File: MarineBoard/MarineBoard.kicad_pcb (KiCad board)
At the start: 4 copper layers, 83 x 67.5 mm, 157 parts, among them CN1 MKDSN 1,5/ 2-5,08, CN2 MKDSN 1,5/ 2-5,08, CN3 SM04B-SRSS-TB (LF)(SN), J1 USB_C_Receptacle_USB2.0_16P, Q2 S8050, Q3 S8050, Q4 BUK762R4-60E, U1 SY8089A1AAC, U10 SM10B-GHS-TB, U11 SN65HVD230DR, U12 DB125-3.5-3P-GN-S, U13 DB125-3.5-3P-GN-S, U14 PC817C-S, U16 PC817C-S, U17 PC817C-S, U18 INA226, U19 INA226, U2 INA226, U21 PC817C-S, U22 SN74LVC1G14DBVR, U23 MCP1407-E/MF_C640313, U3 TPS5430DDA, U4 DB125-3.5-2P-GN-S, U5 DB125-3.5-2P-GN-S, U6 DB125-3.5-2P-GN-S, U7 DB125-3.5-3P-GN-S, U8 ESP32-S3-WROOM-2-N32R16V, U9 DB125-3.5-3P-GN-S

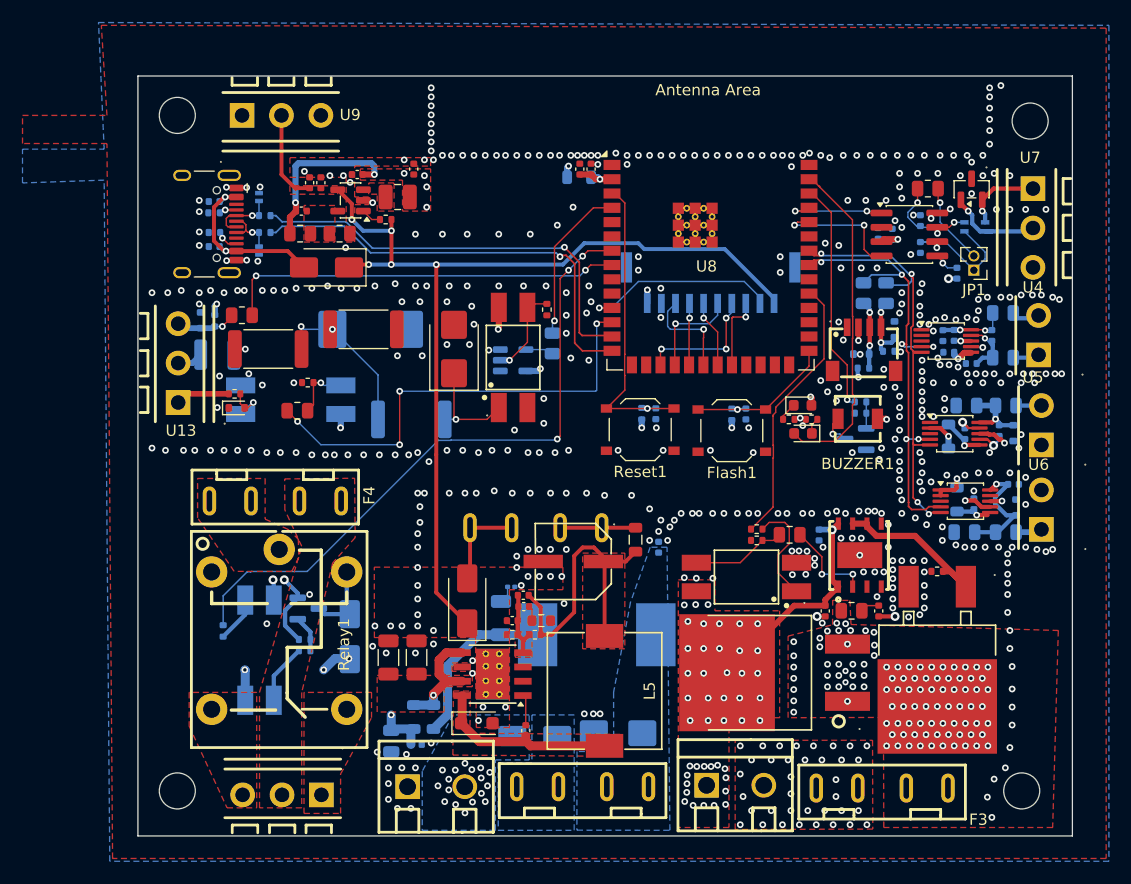
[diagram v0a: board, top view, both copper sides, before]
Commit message: MarineBoard v1.9: RGB status LED, vertical CN4 display header, logo, fab package (#179)
- D17 plain LED -> D5 WS2812B-2020-V6 (C52917434) on GPIO1, VDD +5V_VCC,
  C40 decoupling, R34 100R on DIN
- U10 right-angle GH on the bottom -> CN4 vertical BM10B-GHS-TBT on top
  (pinout unchanged); all fuses/connectors on top; GND stitching reworked
- Sisu logo + "MARINE BOARD v1.9" silk (LOGO1), RESET/FLASH labels
- Libraries consolidated back into Lib/ (root EasyEDA.* retired), CN4
  courtyard now covers its leads, L2 footprint attr THT -> SMD
- fab_package.py rebuilds production/ (DRC gate, gerbers/drill/IPC zip,
  BOM + centroid CSV/XLSX with LOOSE rows); stale production files removed
- Technical Specs v1.9 (CN4, RGB LED, fab script, U5/U6/U7 pin order),
  system spec 2.15, README, feature map, HEADER PINS / LEDS exports

Firmware follow-up for the RGB LED: #180

Co-Authored-By: Claude Opus 5.5 <noreply@anthropic.com>
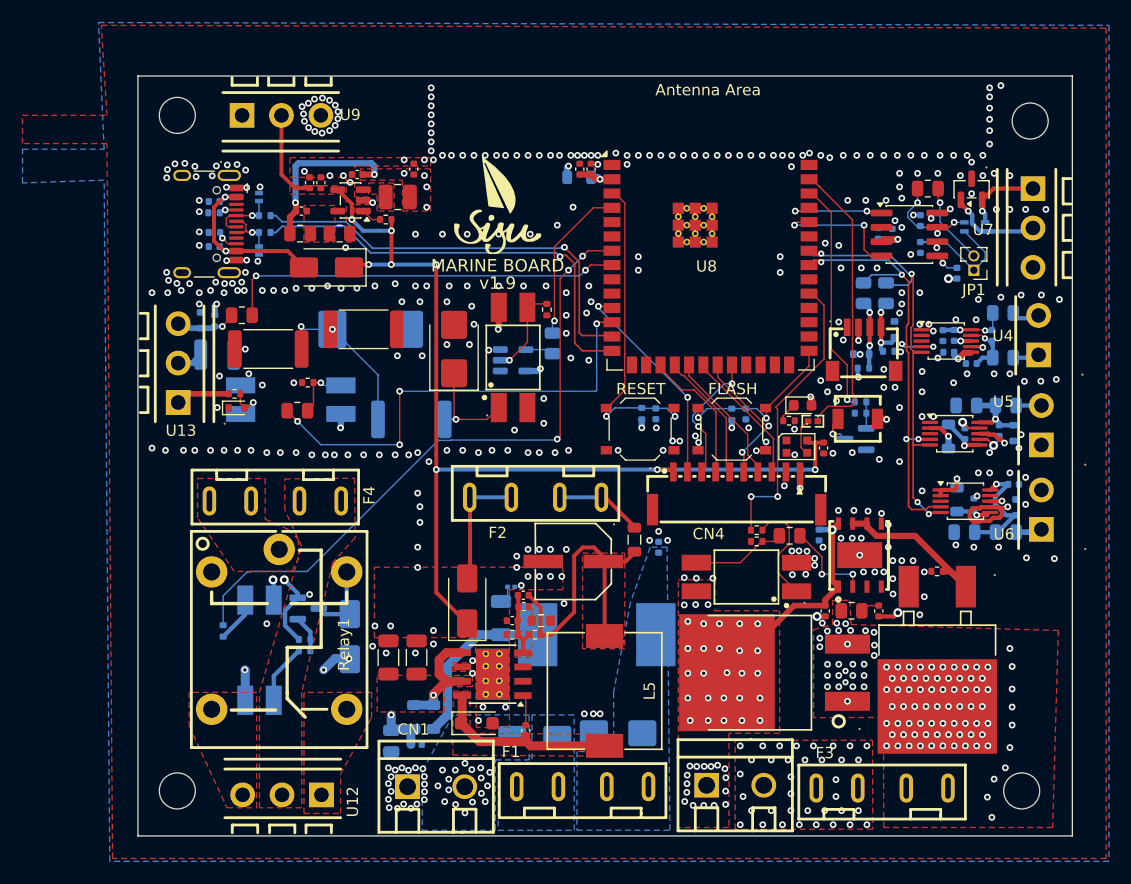
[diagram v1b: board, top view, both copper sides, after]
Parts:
- removed D17: LED, LED_SMD:LED_0603_1608Metric
- removed U10: SM10B-GHS-TB, LCSC:CONN-SMD_SM10B-GHS-TB
- added C40: 0.1uF, Capacitor_SMD:C_0402_1005Metric, F.Cu at (254.7, 70.8)
- added CN4: BM10B-GHS-TBT, LCSC:CONN-SMD_BM10B-GHS-TBT-LF-SN, F.Cu at (246.9, 74.6)
- added D5: WS2812B-2020, LED_SMD:LED_WS2812B-2020_PLCC4_2.0x2.0mm, F.Cu at (252.3, 70.7)
- added LOGO1: v1.9, LCSC:Sisu_Logo, F.Cu at (225.7, 50.8)
- F2: moved to F.Cu
- R34: value 470R -> 100; footprint Resistor_SMD:R_0402_1005Metric -> LCSC:R0402
- moved F2 2.71 mm to (229.1, 75.2)
- moved R34 0.20 mm to (253.7, 68.4), turned to 0 degrees
- moved Flash1 0.14 mm to (246.5, 69.1)
- moved R33 0.12 mm to (251.6, 68.4)
- moved L6 0.10 mm to (237.8, 78.9)
- moved R29 0.09 mm to (248.7, 78.1)
- moved R32 0.09 mm to (248.7, 79.1)
- moved R50 0.09 mm to (251.6, 78.6)
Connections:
- R34 pad 2: GND -> LED
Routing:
- net GND: track 18.4 -> 25.0 mm, vias 478 -> 417
- net MISO/GPIO13: track 5.98 -> 12.5 mm, vias 1 -> 2
- net MOSI/GPIO11: track 5.48 -> 11.9 mm, vias 1 -> 0
- net +5V_VCC: track 93.7 -> 99.5 mm, vias 5 -> 8
- net RST/GPIO14: track 6.64 -> 11.9 mm, vias 1 -> 2
- net LED: track 29.8 -> 26.0 mm
- net SCK/GPIO12: track 8.81 -> 12.0 mm, vias 1 -> 0
- net CS0/GPIO10: track 8.79 -> 11.5 mm, vias 1 -> 0
- net 5V_FUSED: track 8.30 -> 11.0 mm
- net Net-(D5-DIN): track 1.45 -> 3.39 mm
- net BL/GPIO18: track 17.5 -> 19.2 mm, vias 1 -> 2
- net BOOT: track 13.6 -> 15.1 mm, vias 1 -> 2
- net PWM1_GPIO: track 24.4 -> 25.9 mm, vias 0 -> 2
- net RESET: track 27.2 -> 28.6 mm, vias 1 -> 2
- net 5V_FILT: track 6.70 -> 7.85 mm
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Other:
- board text added: "FLASH"
- board text added: "RESET"

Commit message: MarineBoard v1.9.1 pre-fab fixes: U3 ENA float, 50V caps, polymer C20 (#183)
- U3 TPS5430 ENA (pin 5) disconnected from VIN_BUCK (7 V abs max) and left
  floating per TI; schematic wires + PCB stub removed, no-connect added.
- C11/C12/C14/C19/C42 -> CL05B104KB5NNNC (50 V; were 16 V on 12 V/bus nets),
  C33 -> 1 uF 50 V GRM155R61H105KE05D (was 4.7 uF 10 V on +12V BAT).
- C20 -> Panasonic 10SVPE220M 20 mOhm polymer: 15 uH + 220 uF <=40 mOhm is
  TI's internal-compensation reference; the copied ceramic-cap network
  C21/C22/R13/C23 (TI Fig 7-11, 3.3 V/100 uF design) is now DNP.
- Order sheet File Name -> MarineBoard-PCBWay-Gerbers.zip.
- Fab package rebuilt; DRC (schematic parity) and ERC unchanged vs before.

Still open in #183 (routing, human): U2 VBUS, U23 supply rail, C15, D5.

Co-Authored-By: Claude Opus 5.5 <noreply@anthropic.com>
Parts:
- C33: value 4.7uF -> 1uF
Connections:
- U3 pad 5: VIN_BUCK -> unconnected-(U3-EN-Pad5)
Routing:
- net VIN_BUCK: track 10.2 -> 5.75 mm
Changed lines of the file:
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@@
 			)
 		)
-		(property "Value" "4.7uF"
+		(property "Value" "1uF"
 			(at 0 1.16 90)
 			(layer "F.Fab")
@@
 			)
 		)
-		(property "Datasheet" "https://lcsc.com/product-detail/Multilayer-Ceramic-Capacitors-MLCC-SMD-SMT_SAMSUNG_CL05A475MP5NRNC_4-7uF-475-20-10V_C23733.html"
+		(property "Datasheet" "~"
 			(at 0 0 90)
 			(layer "F.Fab")
@@
 			)
 		)
-		(property "Description" "4.7uF ±20% 10V Ceramic Capacitor X5R 0402"
+		(property "Description" "1uF ±10% 50V Ceramic Capacitor X5R 0402"
 			(at 0 0 90)
 			(layer "F.Fab")
@@
 			)
 		)
-		(property "MPN" "CL05A475MP5NRNC"
+		(property "MPN" "GRM155R61H105KE05D"
 			(at 0 0 90)
 			(unlocked yes)
@@
 			)
 		)
-		(property "Manufacturer" "Samsung Electro-Mechanics"
+		(property "Manufacturer" "muRata"
 			(at 0 0 90)
 			(unlocked yes)
@@
 			(size 1.55 0.6)
 			(layers "F.Cu" "F.Mask" "F.Paste")
-			(net "VIN_BUCK")
+			(net "unconnected-(U3-EN-Pad5)")
 			(pinfunction "EN_5")
 			(pintype "input")
@@
 			)
 		)
-		(property "Datasheet" ""
+		(property "Datasheet" "~"
 			(at 0 0 0)
 			(layer "F.Fab")
@@
 			)
 		)
-		(property "Description" "220uF ±20% 10V Aluminum Electrolytic Capacitor 6.3x5.4mm"
+		(property "Description" "220uF ±20% 10V OS-CON polymer, ESR 20mΩ, SMD D6.3xL5.9mm (TPS5430 internal comp needs ESR <=40mΩ)"
 			(at 0 0 0)
 			(layer "F.Fab")
@@
 			)
 		)
-		(property "Manufacturer" "Lelon"
+		(property "Manufacturer" "Panasonic"
 			(at 0 0 180)
 			(unlocked yes)
@@
 			)
 		)
-		(property "MPN" "C72494"
+		(property "MPN" "10SVPE220M"
 			(at 0 0 180)
 			(unlocked yes)
@@
 			)
 		)
-		(attr smd)
+		(attr smd exclude_from_pos_files dnp)
 		(duplicate_pad_numbers_are_jumpers no)
 		(fp_line
@@
 			)
 		)
-		(attr smd)
+		(attr smd exclude_from_pos_files dnp)
 		(duplicate_pad_numbers_are_jumpers no)
 		(fp_line
@@
 			)
 		)
-		(attr smd)
+		(attr smd exclude_from_pos_files dnp)
 		(duplicate_pad_numbers_are_jumpers no)
 		(fp_line
@@
 			)
 		)
-		(attr smd)
+		(attr smd exclude_from_pos_files dnp)
 		(duplicate_pad_numbers_are_jumpers no)
 		(fp_line
@@
 			)
 		)
-		(property "Datasheet" "https://www.lcsc.com/datasheet/C1525.pdf"
+		(property "Datasheet" "~"
 			(at 0 0 90)
 			(layer "B.Fab")
@@
 			)
 		)
-		(property "Description" "Unpolarized capacitor"
+		(property "Description" "100nF ±10% 50V Ceramic Capacitor X7R 0402"
 			(at 0 0 90)
 			(layer "B.Fab")
@@
 			)
 		)
-		(property "MPN" "CL05B104KO5NNNC"
+		(property "MPN" "CL05B104KB5NNNC"
 			(at 0 0 270)
 			(unlocked yes)
@@
 			)
 		)
-		(property "Datasheet" "https://www.lcsc.com/datasheet/C1525.pdf"
+		(property "Datasheet" "~"
 			(at 0 0 90)
 			(layer "B.Fab")
@@
 			)
 		)
-		(property "Description" "Unpolarized capacitor"
+		(property "Description" "100nF ±10% 50V Ceramic Capacitor X7R 0402"
 			(at 0 0 90)
 			(layer "B.Fab")
@@
 			)
 		)
-		(property "MPN" "CL05B104KO5NNNC"
+		(property "MPN" "CL05B104KB5NNNC"
 			(at 0 0 90)
 			(unlocked yes)
@@
 			)
 		)
-		(property "Datasheet" ""
+		(property "Datasheet" "~"
 			(at 0 0 90)
 			(layer "B.Fab")
@@
 			)
 		)
-		(property "MPN" "CL05B104KO5NNNC"
+		(property "MPN" "CL05B104KB5NNNC"
 			(at 0 0 90)
 			(unlocked yes)
@@
 			)
 		)
-		(property "Datasheet" "https://www.lcsc.com/datasheet/C1525.pdf"
+		(property "Datasheet" "~"
 			(at 0 0 0)
 			(layer "B.Fab")
@@
 			)
 		)
-		(property "Description" "Unpolarized capacitor"
+		(property "Description" "100nF ±10% 50V Ceramic Capacitor X7R 0402"
 			(at 0 0 0)
 			(layer "B.Fab")
@@
 			)
 		)
-		(property "MPN" "CL05B104KO5NNNC"
+		(property "MPN" "CL05B104KB5NNNC"
 			(at 0 0 180)
 			(unlocked yes)
@@
 			)
 		)
-		(property "Datasheet" "https://www.lcsc.com/datasheet/C1525.pdf"
+		(property "Datasheet" "~"
 			(at 0 0 0)
 			(layer "B.Fab")
@@
 			)
 		)
-		(property "Description" "Unpolarized capacitor"
+		(property "Description" "100nF ±10% 50V Ceramic Capacitor X7R 0402"
 			(at 0 0 0)
 			(layer "B.Fab")
@@
 			)
 		)
-		(property "MPN" "CL05B104KO5NNNC"
+		(property "MPN" "CL05B104KB5NNNC"
 			(at 0 0 180)
 			(unlocked yes)
@@
 	)
 	(segment
-		(start 221.155 88.97)
-		(end 220.5 89.625)
-		(width 0.8)
-		(layer "F.Cu")
-		(net "VIN_BUCK")
-	)
-	(segment
-		(start 222.55 88.97)
-		(end 221.155 88.97)
-		(width 0.8)
-		(layer "F.Cu")
-		(net "VIN_BUCK")
-	)
-	(segment
 		(start 220 92.75)
 		(end 220 92.645)
 		(width 0.8)
 		(layer "F.Cu")
-		(net "VIN_BUCK")
-	)
-	(segment
-		(start 220.5 90.875)
-		(end 221.135 91.51)
-		(width 0.8)
-		(layer "F.Cu")
-		(net "VIN_BUCK")
-	)
-	(segment
-		(start 220.5 89.625)
-		(end 220.5 90.875)
-		(width 0.8)
-		(layer "F.Cu")

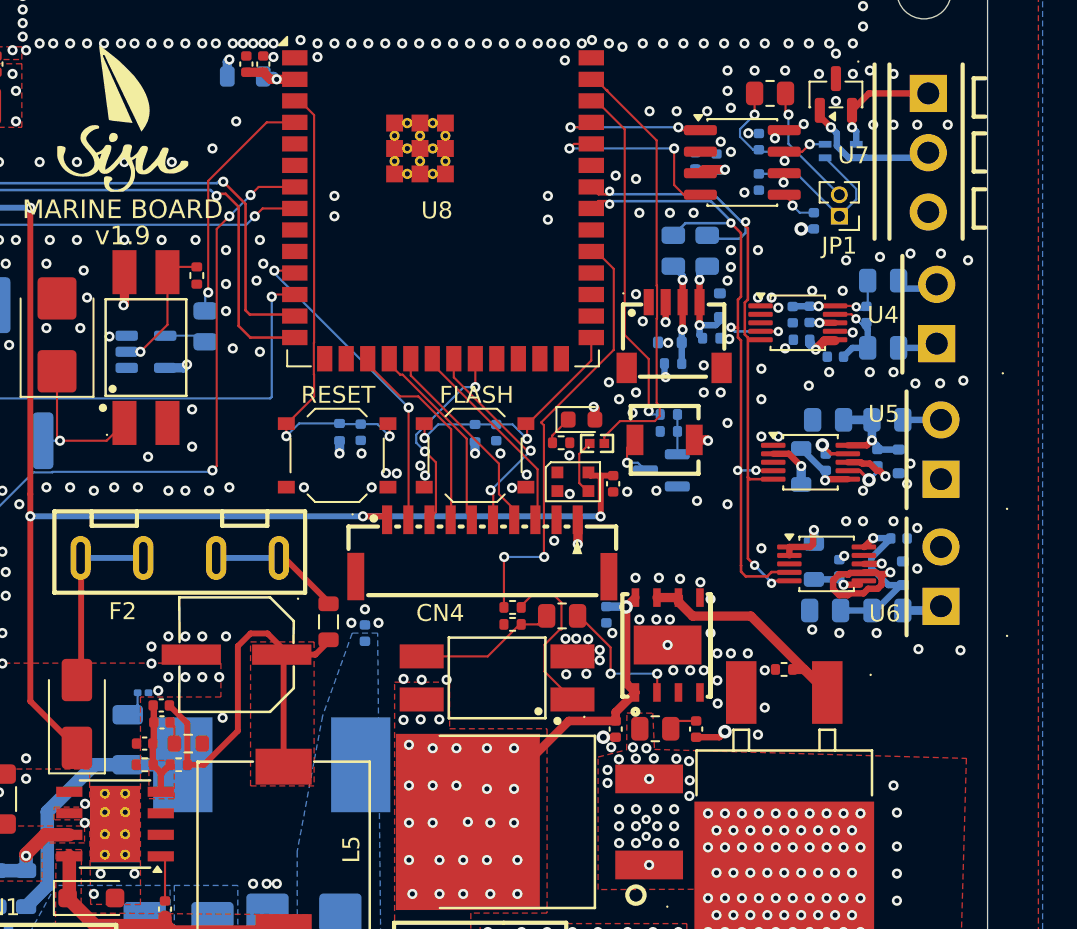
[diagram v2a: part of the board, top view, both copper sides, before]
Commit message: MarineBoard 1.9.1: routed PCB + fab package rebuilt (#183)
PCB updated from the d7f7e75 schematic and routed (human): D17 buzzer
flyback, D21 D5 VDD diode (bottom), TP1-TP6 test pads, U23 VDD on +12V,
U2 VBUS=Vin+, CAN on GPIO5/6; removed C10/C21-C23/R13.
fab_package.py green: DRC errors 0, unconnected 0, schematic parity 0
(8 silkscreen warnings only). BOM/positions: D17/D21 in, TPs and removed
parts out. Ready for PCBWay re-upload.

Co-Authored-By: Claude Opus 5.5 <noreply@anthropic.com>
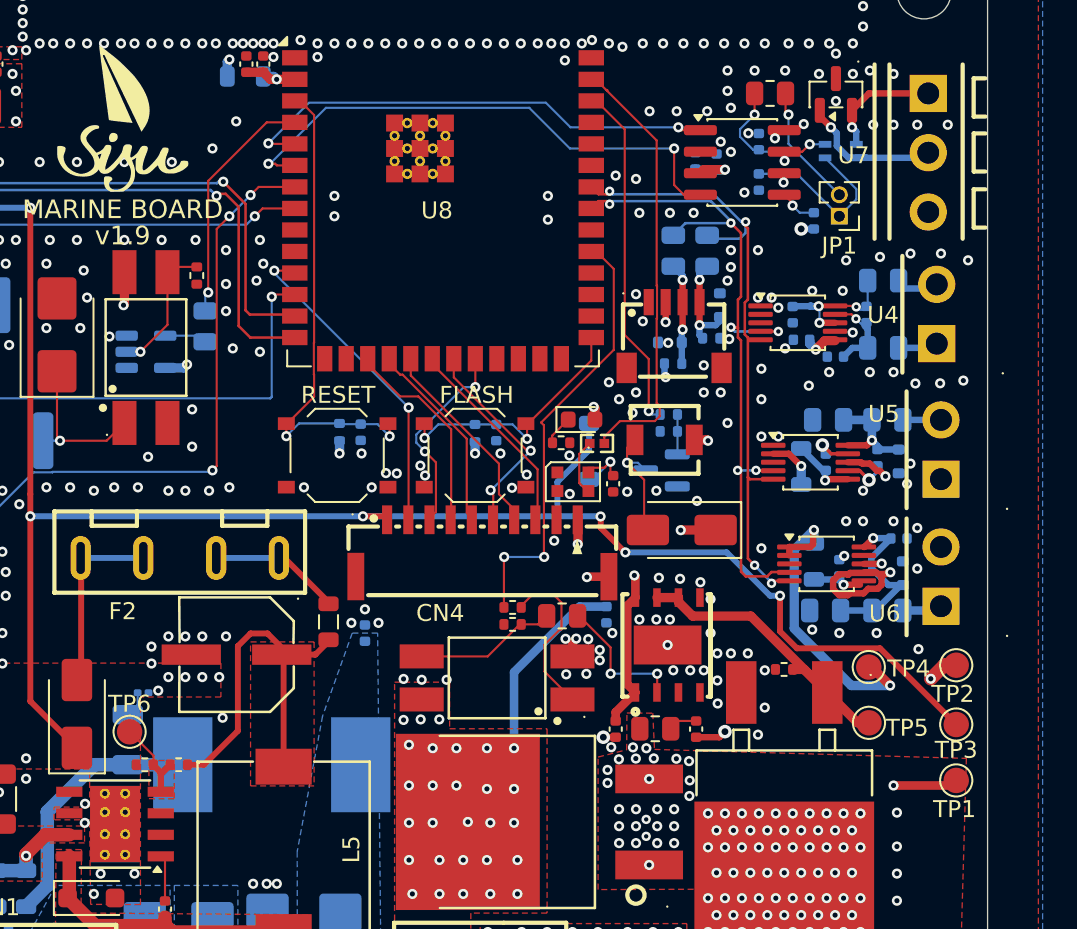
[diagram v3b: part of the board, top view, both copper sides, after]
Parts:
- removed C10: 4.7uF, Capacitor_SMD:C_0402_1005Metric
- removed C21: 1.5nF, Capacitor_SMD:C_0402_1005Metric
- removed C22: 0.1uF, Capacitor_SMD:C_0402_1005Metric
- removed C23: 150pF, Capacitor_SMD:C_0402_1005Metric
- removed R13: 549, Resistor_SMD:R_0603_1608Metric
- added D17: SS14, Diode_SMD:D_SMA, F.Cu at (258.7, 73.5)
- added D21: 1N4148W, Diode_SMD:D_SOD-123, B.Cu at (253.2, 68.9)
- added TP1: GND, TestPoint:TestPoint_Pad_D1.5mm, F.Cu at (274.9, 88.3)
- added TP2: +12V, TestPoint:TestPoint_Pad_D1.5mm, F.Cu at (274.9, 81.5)
- added TP3: +5V_VCC, TestPoint:TestPoint_Pad_D1.5mm, F.Cu at (274.9, 85.0)
- added TP4: +3.3V, TestPoint:TestPoint_Pad_D1.5mm, F.Cu at (269.7, 81.6)
- added TP5: PWM_GATE, TestPoint:TestPoint_Pad_D1.5mm, F.Cu at (269.8, 84.9)
- added TP6: VSENSE, TestPoint:TestPoint_Pad_D1.5mm, F.Cu at (226.1, 85.4)
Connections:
- net Net-(U3-VSENSE) renamed VSENSE
- C12 pad 1: Net-(U2-Vin+) -> Net-(U2-Vbus)
- C33 pad 2: +12V BAT -> +12V
- C40 pad 2: +5V_VCC -> Net-(D21-K)
- C9 pad 2: Net-(U2-Vin+) -> Net-(U2-Vbus)
- D5 pad 4: +5V_VCC -> Net-(D21-K)
- R7 pad 2: Net-(U2-Vin+) -> Net-(U2-Vbus)
- U2 pad 10: Net-(U2-Vin+) -> Net-(U2-Vbus)
- U23 pad 1: +12V BAT -> +12V
- U23 pad 8: +12V BAT -> +12V
- U8 pad 36: CAN RX_GPIO -> unconnected-(U8-U0RXD/GPIO44/CLK_OUT2-Pad36)
- U8 pad 37: CAN TX_GPIO -> unconnected-(U8-U0TXD/GPIO43/CLK_OUT1-Pad37)
- U8 pad 5: unconnected-(U8-GPIO5/TOUCH5/ADC1_CH4-Pad5) -> CAN TX_GPIO
- U8 pad 6: unconnected-(U8-GPIO6/TOUCH6/ADC1_CH5-Pad6) -> CAN RX_GPIO
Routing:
- net +5V_VCC: track 99.5 -> 129.6 mm, vias 8 -> 10
- net CAN RX_GPIO: track 11.5 -> 31.9 mm
- net CAN TX_GPIO: track 9.09 -> 28.7 mm
- net +3.3V: track 41.2 -> 58.1 mm, vias 23 -> 25
- net +12V: track 14.0 -> 25.3 mm, vias 6 -> 8
- net +12V BAT: track 20.6 -> 11.5 mm, vias 65 -> 64
- net Net-(U2-Vbus): track 1.51 -> 8.26 mm, vias 1 -> 3
- net Net-(U2-Vin+): track 6.31 -> 0.00 mm, vias 2 -> 0
- net GND: track 25.0 -> 31.3 mm, vias 417 -> 415
- net Net-(BUZZER1--): track 2.82 -> 7.21 mm
- net Net-(D21-K): track 0.00 -> 4.29 mm, vias 0 -> 1
- net 5V_BUCK: track 25.9 -> 21.9 mm
- net PWM_GATE: track 15.1 -> 18.3 mm
- net Net-(C22-Pad2): track 1.35 -> 0.00 mm
- net VSENSE: track 6.20 -> 5.23 mm
